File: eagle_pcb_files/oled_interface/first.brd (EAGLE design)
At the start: 36.8 x 35.2 mm, 8 parts

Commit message: Upgraded OLED Board
New board for fast manufacturing
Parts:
- added BME680: (no value), pinhead:1X05
- renumbered JP1 to SDA
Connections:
- net N$5 renamed B3
- net N$6 renamed B2
- net N$7 renamed B1
- removed net N$1: R1.2, R2.2, R3.2, SDA.2, U$1.2
- removed net N$2: S1.1, S2.1, S3.1, SDA.1, U$1.1
- removed net N$3: SDA.3, U$1.3
- new net GND: BME680.5, R1.2, R2.2, R3.2, SDA.2, U$1.2
- new net SCL: BME680.3, SDA.3, U$1.3
- new net VCC: BME680.1, S1.1, S2.1, S3.1, SDA.1, U$1.1
- net N$4: now also BME680.2
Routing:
- net VCC: track 0.00 -> 64.8 mm
- net N$1: track 60.2 -> 0.00 mm, vias 4 -> 0
- net N$2: track 59.0 -> 0.00 mm
- net N$4: track 7.47 -> 28.8 mm
- net SCL: track 0.00 -> 15.4 mm
- net N$3: track 7.47 -> 0.00 mm

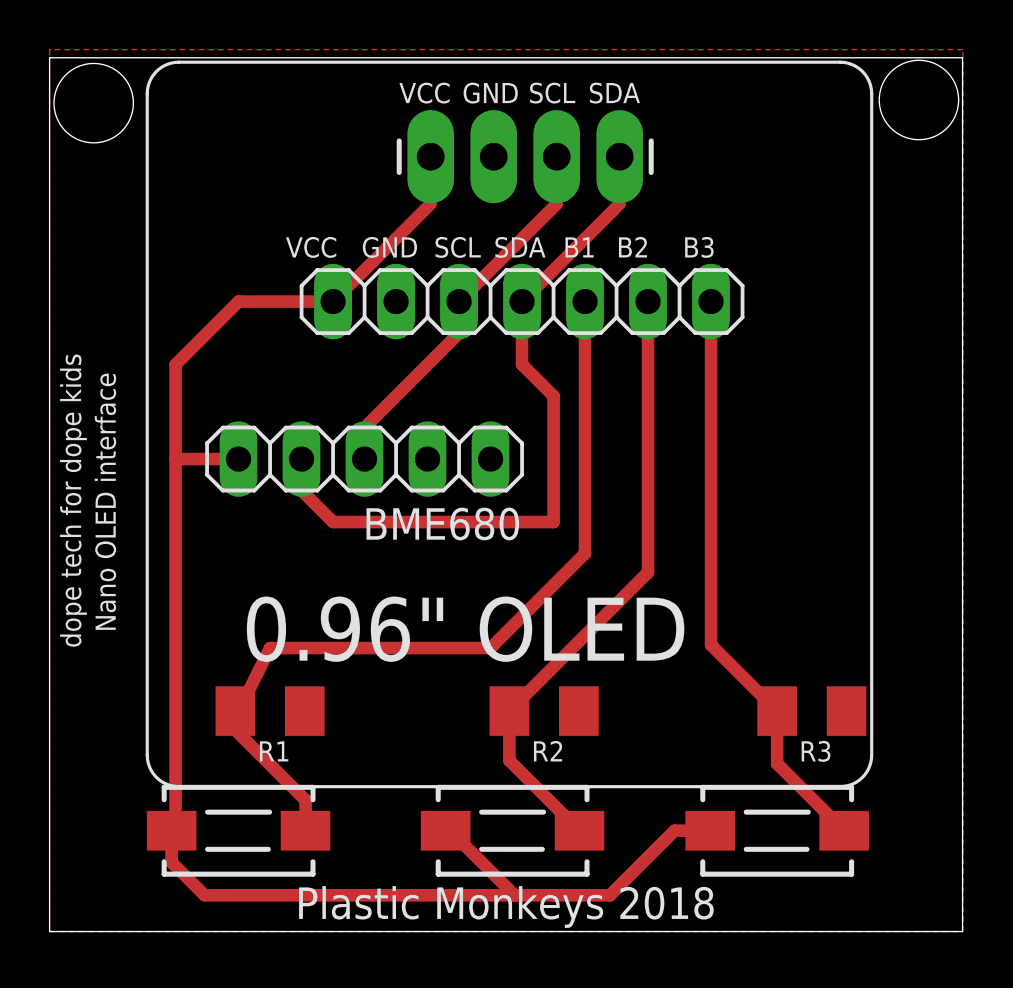
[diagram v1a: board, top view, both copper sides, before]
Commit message: New Buttons Pads
previous was too small for our buttons
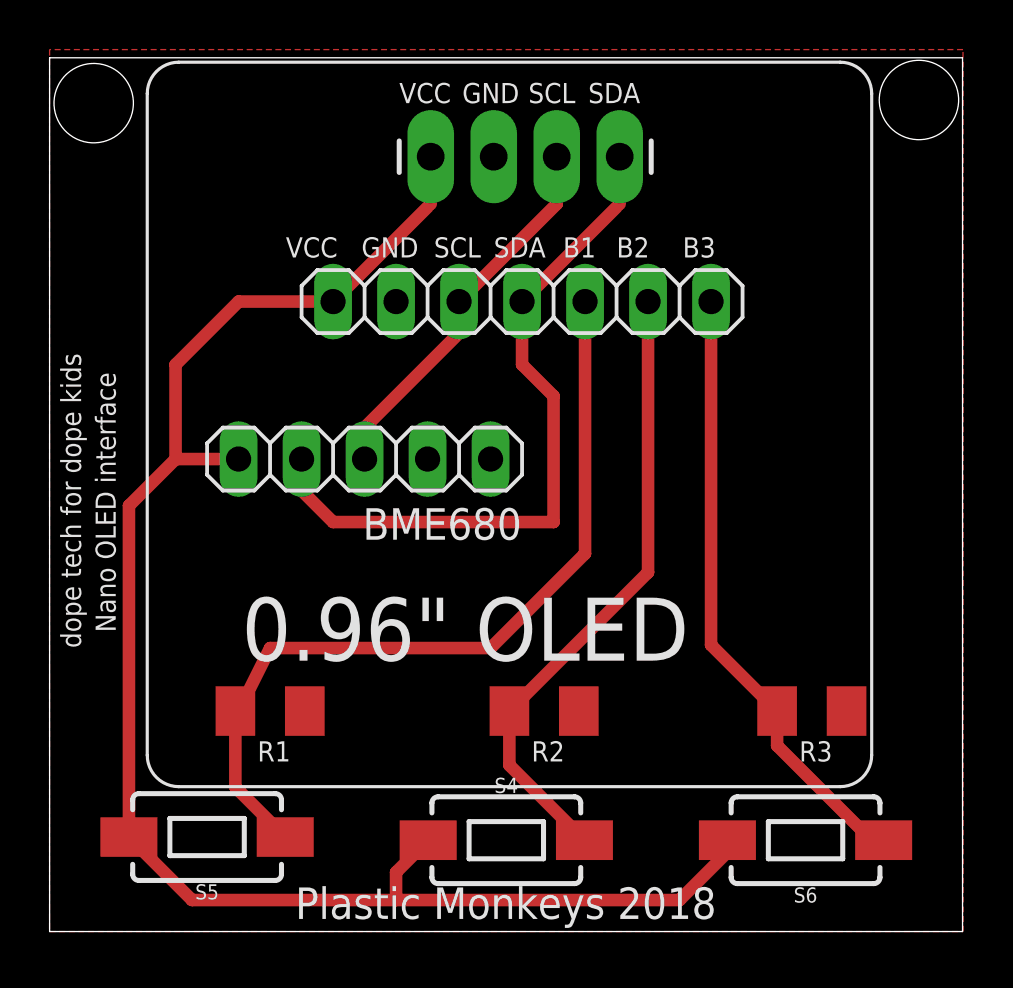
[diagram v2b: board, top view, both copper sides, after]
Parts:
- removed S1, S2, S3: DTSM-3, switch-tact:DTSM-3
- added S4, S5, S6: MOMENTARY-SWITCH-SPST-SMD-6.0X3.5MM, SparkFun-Switches:TACTILE_SWITCH_SMD_6.0X3.5MM
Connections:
- net B1: now also S5.1; no longer S3.2
- net B2: now also S4.2; no longer S1.2
- net B3: now also S6.1; no longer S2.2
- net VCC: now also S4.1, S5.2, S6.2; no longer S1.1, S2.1, S3.1
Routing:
- net VCC: track 64.8 -> 66.7 mm
- net B3: track 23.6 -> 24.9 mm
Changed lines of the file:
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@@
 <layer number="21" name="tPlace" color="7" fill="1" visible="no" active="yes"/>
 <layer number="22" name="bPlace" color="7" fill="1" visible="no" active="yes"/>
-<layer number="23" name="tOrigins" color="15" fill="1" visible="no" active="yes"/>
+<layer number="23" name="tOrigins" color="15" fill="1" visible="yes" active="yes"/>
 <layer number="24" name="bOrigins" color="15" fill="1" visible="no" active="yes"/>
 <layer number="25" name="tNames" color="7" fill="1" visible="no" active="yes"/>
@@
 <elements>
 <element name="U$1" library="DIYMall_OLED" package="I2C_OLED_PACKAGE" value="I2C_OLED" x="15.367" y="31.242" smashed="yes"/>
-<element name="S1" library="switch-tact" package="DTSM-3" value="DTSM-3" x="18.669" y="4.064" smashed="yes"/>
-<element name="S2" library="switch-tact" package="DTSM-3" value="DTSM-3" x="29.337" y="4.064" smashed="yes"/>
-<element name="S3" library="switch-tact" package="DTSM-3" value="DTSM-3" x="7.62" y="4.064" smashed="yes"/>
 <element name="R1" library="rcl" library_urn="urn:adsk.eagle:library:334" package="M1206" package3d_urn="urn:adsk.eagle:package:23566/1" value="" x="19.939" y="8.89" smashed="yes">
 <attribute name="SPICEPREFIX" value="10K" x="19.939" y="8.89" size="1.778" layer="27" display="off"/>
@@
 <attribute name="NAME" x="12.6238" y="15.7988" size="1.27" layer="25" ratio="10"/>
 <attribute name="VALUE" x="6.35" y="15.875" size="1.27" layer="27"/>
+</element>
+<element name="S4" library="SparkFun-Switches" package="TACTILE_SWITCH_SMD_6.0X3.5MM" value="MOMENTARY-SWITCH-SPST-SMD-6.0X3.5MM" x="18.415" y="3.683" smashed="yes">
+<attribute name="NAME" x="18.415" y="5.588" size="0.6096" layer="25" font="vector" ratio="20" align="bottom-center"/>
+<attribute name="PROD_ID" value="SWCH-00815" x="18.415" y="3.683" size="1.778" layer="27" display="off"/>
+<attribute name="SF_SKU" value="COM-08229" x="18.415" y="3.683" size="1.778" layer="27" display="off"/>
+<attribute name="VALUE" x="18.415" y="1.778" size="0.6096" layer="27" font="vector" ratio="20" align="top-center"/>
+</element>
+<element name="S5" library="SparkFun-Switches" package="TACTILE_SWITCH_SMD_6.0X3.5MM" value="MOMENTARY-SWITCH-SPST-SMD-6.0X3.5MM" x="6.35" y="3.81" smashed="yes" rot="R180">
+<attribute name="NAME" x="6.35" y="1.905" size="0.6096" layer="25" font="vector" ratio="20" rot="R180" align="bottom-center"/>
+<attribute name="PROD_ID" value="SWCH-00815" x="6.35" y="3.81" size="1.778" layer="27" rot="R180" display="off"/>
+<attribute name="SF_SKU" value="COM-08229" x="6.35" y="3.81" size="1.778" layer="27" rot="R180" display="off"/>
+<attribute name="VALUE" x="6.35" y="5.715" size="0.6096" layer="27" font="vector" ratio="20" rot="R180" align="top-center"/>
+</element>
+<element name="S6" library="SparkFun-Switches" package="TACTILE_SWITCH_SMD_6.0X3.5MM" value="MOMENTARY-SWITCH-SPST-SMD-6.0X3.5MM" x="30.48" y="3.683" smashed="yes" rot="R180">
+<attribute name="NAME" x="30.48" y="1.778" size="0.6096" layer="25" font="vector" ratio="20" rot="R180" align="bottom-center"/>
+<attribute name="PROD_ID" value="SWCH-00815" x="30.48" y="3.683" size="1.778" layer="27" rot="R180" display="off"/>
+<attribute name="SF_SKU" value="COM-08229" x="30.48" y="3.683" size="1.778" layer="27" rot="R180" display="off"/>
+<attribute name="VALUE" x="30.48" y="5.588" size="0.6096" layer="27" font="vector" ratio="20" rot="R180" align="top-center"/>
 </element>
 </elements>
@@
 </signal>
 <signal name="B3">
-<contactref element="S2" pad="2"/>
 <contactref element="R3" pad="1"/>
 <contactref element="SDA" pad="7"/>
-<wire x1="32.037" y1="4.064" x2="29.334" y2="6.767" width="0.508" layer="1"/>
-<wire x1="29.334" y1="6.767" x2="29.334" y2="8.89" width="0.508" layer="1"/>
 <wire x1="26.67" y1="11.554" x2="29.334" y2="8.89" width="0.508" layer="1"/>
 <wire x1="26.67" y1="25.4" x2="26.67" y2="11.554" width="0.508" layer="1"/>
+<contactref element="S6" pad="1"/>
+<wire x1="29.334" y1="8.89" x2="29.334" y2="7.496" width="0.508" layer="1"/>
+<wire x1="33.147" y1="3.683" x2="33.63" y2="3.683" width="0.508" layer="1"/>
+<wire x1="29.334" y1="7.496" x2="33.147" y2="3.683" width="0.508" layer="1"/>
 </signal>
 <signal name="B2">
-<contactref element="S1" pad="2"/>
 <contactref element="R1" pad="1"/>
 <contactref element="SDA" pad="6"/>
 <wire x1="24.13" y1="25.4" x2="24.13" y2="14.481" width="0.508" layer="1"/>
 <wire x1="24.13" y1="14.481" x2="18.539" y2="8.89" width="0.508" layer="1"/>
-<wire x1="18.539" y1="8.89" x2="18.539" y2="6.894" width="0.508" layer="1"/>
-<wire x1="18.539" y1="6.894" x2="21.369" y2="4.064" width="0.508" layer="1"/>
+<contactref element="S4" pad="2"/>
+<wire x1="18.539" y1="8.89" x2="18.539" y2="6.709" width="0.508" layer="1"/>
+<wire x1="18.539" y1="6.709" x2="21.565" y2="3.683" width="0.508" layer="1"/>
 </signal>
 <signal name="B1">
-<contactref element="S3" pad="2"/>
 <contactref element="R2" pad="1"/>
 <contactref element="SDA" pad="5"/>
 <wire x1="7.49" y1="8.89" x2="7.555" y2="8.825" width="0.1524" layer="1"/>
-<wire x1="7.174" y1="8.444" x2="10.32" y2="5.298" width="0.508" layer="1"/>
-<wire x1="10.32" y1="5.298" x2="10.32" y2="4.064" width="0.508" layer="1"/>
 <wire x1="21.59" y1="25.4" x2="21.59" y2="15.24" width="0.508" layer="1"/>
 <wire x1="21.59" y1="15.24" x2="17.78" y2="11.43" width="0.508" layer="1"/>
@@
 <wire x1="8.89" y1="11.43" x2="7.62" y2="8.89" width="0.508" layer="1"/>
 <wire x1="7.62" y1="8.89" x2="7.555" y2="8.825" width="0.1524" layer="1"/>
-<wire x1="7.555" y1="8.825" x2="7.174" y2="8.444" width="0.1524" layer="1"/>
+<contactref element="S5" pad="1"/>
+<wire x1="7.49" y1="8.89" x2="7.49" y2="5.82" width="0.508" layer="1"/>
+<wire x1="7.49" y1="5.82" x2="9.5" y2="3.81" width="0.508" layer="1"/>
 </signal>
 <signal name="VCC">
-<contactref element="S3" pad="1"/>
-<contactref element="S1" pad="1"/>
-<contactref element="S2" pad="1"/>
 <contactref element="SDA" pad="1"/>
-<wire x1="4.92" y1="4.064" x2="5.08" y2="4.064" width="0.1524" layer="1"/>
-<wire x1="20.32" y1="1.4606" x2="22.58994375" y2="1.4606" width="0.508" layer="1"/>
-<wire x1="26.637" y1="4.064" x2="25.19334375" y2="4.064" width="0.508" layer="1"/>
-<wire x1="25.19334375" y1="4.064" x2="22.58994375" y2="1.4606" width="0.508" layer="1"/>
 <wire x1="11.43" y1="25.4" x2="7.62" y2="25.4" width="0.508" layer="1"/>
 <wire x1="7.62" y1="25.4" x2="5.08" y2="22.86" width="0.508" layer="1"/>
 <wire x1="5.08" y1="22.86" x2="5.08" y2="19.05" width="0.508" layer="1"/>
-<wire x1="5.08" y1="19.05" x2="5.08" y2="4.064" width="0.508" layer="1"/>
-<wire x1="15.969" y1="4.064" x2="16.14765625" y2="4.064" width="0.508" layer="1"/>
-<wire x1="16.14765625" y1="4.064" x2="18.75105625" y2="1.4606" width="0.508" layer="1"/>
-<wire x1="4.92" y1="2.794" x2="6.244171875" y2="1.469828125" width="0.508" layer="1"/>
-<wire x1="4.92" y1="4.064" x2="4.92" y2="2.794" width="0.508" layer="1"/>
 <contactref element="U$1" pad="1"/>
 <wire x1="11.43" y1="25.4" x2="15.24" y2="29.21" width="0.508" layer="1"/>
 <wire x1="15.367" y1="29.337" x2="15.24" y2="29.21" width="0.1524" layer="1"/>
 <wire x1="15.367" y1="31.242" x2="15.367" y2="29.337" width="0.508" layer="1"/>
-<wire x1="6.244171875" y1="1.469828125" x2="6.2534" y2="1.4606" width="0.1524" layer="1"/>
-<wire x1="6.2534" y1="1.4606" x2="18.75105625" y2="1.4606" width="0.508" layer="1"/>
 <contactref element="BME680" pad="1"/>
 <wire x1="7.62" y1="19.05" x2="5.08" y2="19.05" width="0.508" layer="1"/>
-<wire x1="18.75105625" y1="1.4606" x2="20.32" y2="1.4606" width="0.508" layer="1"/>
+<contactref element="S6" pad="2"/>
+<contactref element="S4" pad="1"/>
+<contactref element="S5" pad="2"/>
+<wire x1="5.08" y1="19.05" x2="3.2" y2="17.17" width="0.508" layer="1"/>
+<wire x1="3.2" y1="17.17" x2="3.2" y2="3.81" width="0.508" layer="1"/>
+<wire x1="3.2" y1="3.81" x2="5.74" y2="1.27" width="0.508" layer="1"/>
+<wire x1="5.74" y1="1.27" x2="13.97" y2="1.27" width="0.508" layer="1"/>
+<wire x1="13.97" y1="1.27" x2="13.97" y2="2.388" width="0.508" layer="1"/>
+<wire x1="13.97" y1="2.388" x2="15.265" y2="3.683" width="0.508" layer="1"/>
+<wire x1="13.97" y1="1.27" x2="25.4" y2="1.27" width="0.508" layer="1"/>
+<wire x1="25.4" y1="1.27" x2="27.33" y2="3.2" width="0.508" layer="1"/>
+<wire x1="27.33" y1="3.2" x2="27.33" y2="3.683" width="0.508" layer="1"/>
 </signal>
 <signal name="GND">
@@
 <vertex x="0" y="35.56"/>
 </polygon>
+<wire x1="17.78" y1="19.05" x2="13.97" y2="25.4" width="0" layer="19" extent="1-1"/>
 </signal>
 </signals>
